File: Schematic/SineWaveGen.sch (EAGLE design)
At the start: 16 parts, among them IC1 MEGA32-P, Q1 G20N60, Q2 G20N60, Q3 H9NA80FI, Q4 H9NA80FI

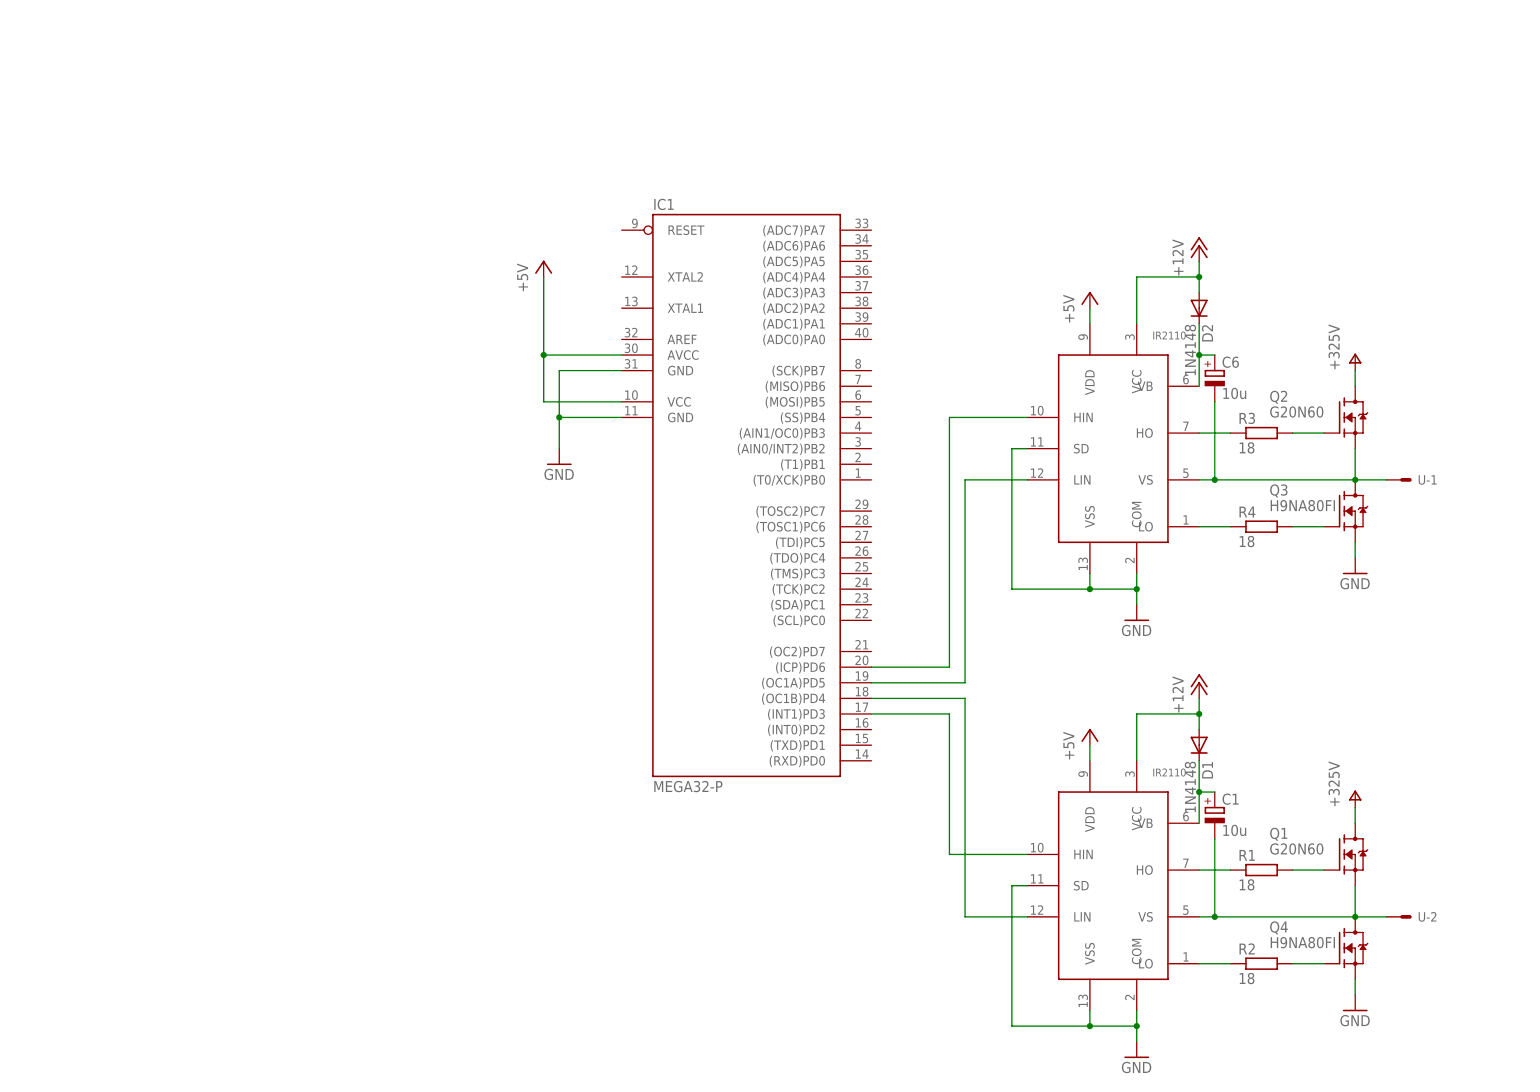
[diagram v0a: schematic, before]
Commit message: use bigger distances for high voltages
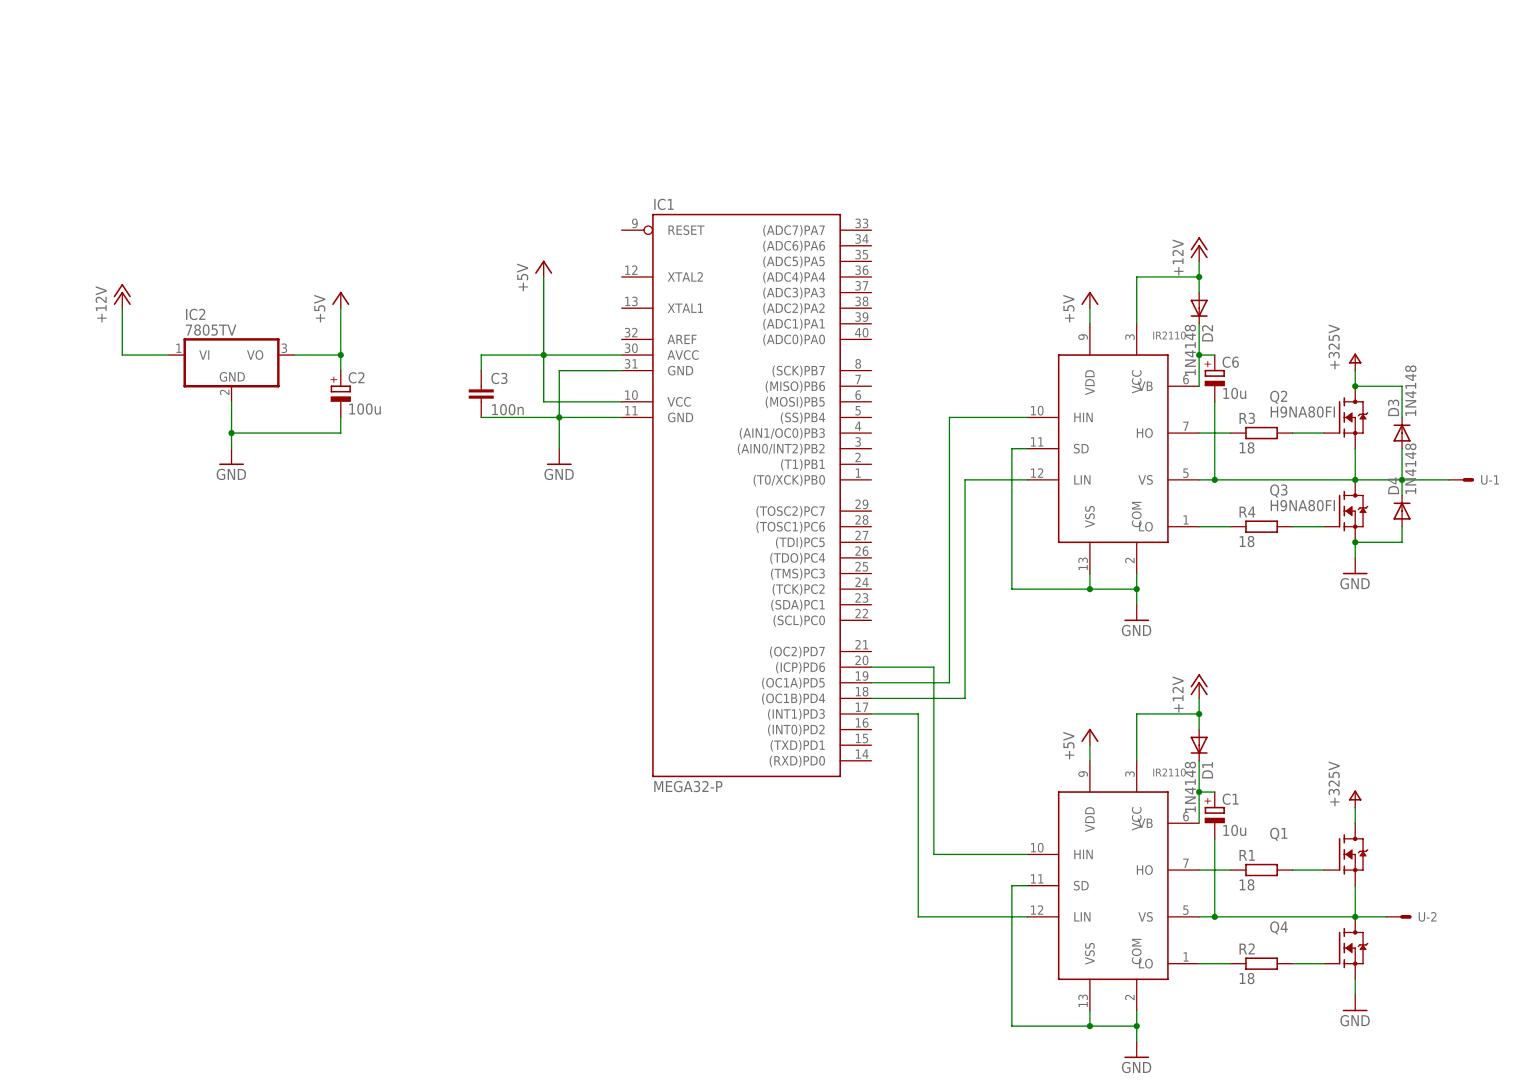
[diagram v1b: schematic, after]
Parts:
- added C2: 100u, rcl:CPOL-EUE2.5-7
- added C3: 100n, rcl:C-EU050-035X075
- added D3, D4: 1N4148, diode:1N4148DO35-7
- added IC2: 7805TV, linear:7805TV
- Q1: value G20N60 -> SPW47N60S5
- Q2: value G20N60 -> H9NA80FI
- Q4: value H9NA80FI -> SPW47N60S5
- R1: device rcl:R-EU_0207/10 -> rcl:R-EU_0207/12
- R3: device rcl:R-EU_0204/2V -> rcl:R-EU_0207/12
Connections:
- net +12V: now also IC2.VI
- net +5V: now also C2.+, C3.1, IC2.VO
- net GND: now also C2.-, C3.2, D4.A, IC2.GND
- net N$10: now also IC1.(INT1)PD3; no longer IC1.(OC1B)PD4
- net N$11: now also IC1.(ICP)PD6; no longer IC1.(INT1)PD3
- net N$2: now also IC1.(OC1B)PD4; no longer IC1.(OC1A)PD5
- net N$32: now also D3.A, D4.C
- net N$4: now also IC1.(OC1A)PD5; no longer IC1.(ICP)PD6
- net V+: now also D3.C
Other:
- moved on the sheet: U-1
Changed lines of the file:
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@@
 <setting verticaltext="up"/>
 </settings>
-<grid distance="0.1" unitdist="inch" unit="inch" style="lines" multiple="1" display="yes" altdistance="0.01" altunitdist="inch" altunit="inch"/>
+<grid distance="0.1" unitdist="inch" unit="inch" style="lines" multiple="1" display="no" altdistance="0.01" altunitdist="inch" altunit="inch"/>
 <layers>
 <layer number="1" name="Top" color="4" fill="1" visible="yes" active="no"/>
@@
 <parts>
 <part name="U$2" library="BLDC" deviceset="IR2110" device="DIL14" value="IR2110"/>
-<part name="Q2" library="transistor-fet" deviceset="SPW47N60S5" device="" value="G20N60"/>
+<part name="Q2" library="transistor-fet" deviceset="SPW47N60S5" device="" value="H9NA80FI"/>
 <part name="Q3" library="transistor-fet" deviceset="SPW47N60S5" device="" value="H9NA80FI"/>
-<part name="R3" library="rcl" deviceset="R-EU_" device="0204/2V" value="18"/>
+<part name="R3" library="rcl" deviceset="R-EU_" device="0207/12" value="18"/>
 <part name="R4" library="rcl" deviceset="R-EU_" device="0207/12" value="18"/>
 <part name="C6" library="rcl" deviceset="CPOL-EU" device="E2.5-7" value="10u"/>
@@
 <part name="P+1" library="supply1" deviceset="+5V" device=""/>
 <part name="U$1" library="BLDC" deviceset="IR2110" device="DIL14" value="IR2110"/>
-<part name="Q1" library="transistor-fet" deviceset="SPW47N60S5" device="" value="G20N60"/>
-<part name="Q4" library="transistor-fet" deviceset="SPW47N60S5" device="" value="H9NA80FI"/>
-<part name="R1" library="rcl" deviceset="R-EU_" device="0207/10" value="18"/>
+<part name="Q1" library="transistor-fet" deviceset="SPW47N60S5" device="" value=""/>
+<part name="Q4" library="transistor-fet" deviceset="SPW47N60S5" device="" value=""/>
+<part name="R1" library="rcl" deviceset="R-EU_" device="0207/12" value="18"/>
 <part name="R2" library="rcl" deviceset="R-EU_" device="0207/12" value="18"/>
 <part name="C1" library="rcl" deviceset="CPOL-EU" device="E2.5-7" value="10u"/>
@@
 <part name="GND4" library="supply1" deviceset="GND" device=""/>
 <part name="GND5" library="supply1" deviceset="GND" device=""/>
+<part name="IC2" library="linear" deviceset="78*" device="TV" technology="05"/>
+<part name="C2" library="rcl" deviceset="CPOL-EU" device="E2.5-7" value="100u"/>
+<part name="P+8" library="supply1" deviceset="+5V" device=""/>
+<part name="P+9" library="supply1" deviceset="+12V" device=""/>
+<part name="GND6" library="supply1" deviceset="GND" device=""/>
+<part name="C3" library="rcl" deviceset="C-EU" device="050-035X075" value="100n"/>
+<part name="D3" library="diode" deviceset="1N4148" device="DO35-7" value="1N4148"/>
+<part name="D4" library="diode" deviceset="1N4148" device="DO35-7" value="1N4148"/>
 </parts>
 <sheets>
@@
 <instance part="R4" gate="G$1" x="58.42" y="60.96"/>
 <instance part="C6" gate="G$1" x="50.8" y="86.36"/>
-<instance part="U" gate="-1" x="81.28" y="68.58"/>
+<instance part="U" gate="-1" x="91.44" y="68.58"/>
 <instance part="U" gate="-2" x="81.28" y="-2.54"/>
 <instance part="IC1" gate="G$1" x="-25.4" y="66.04"/>
@@
 <instance part="GND4" gate="1" x="73.66" y="-17.78"/>
 <instance part="GND5" gate="1" x="38.1" y="-25.4"/>
+<instance part="IC2" gate="A1" x="-109.22" y="88.9"/>
+<instance part="C2" gate="G$1" x="-91.44" y="83.82"/>
+<instance part="P+8" gate="1" x="-91.44" y="99.06"/>
+<instance part="P+9" gate="1" x="-127" y="99.06"/>
+<instance part="GND6" gate="1" x="-109.22" y="71.12"/>
+<instance part="C3" gate="G$1" x="-68.58" y="83.82"/>
+<instance part="D3" gate="G$1" x="81.28" y="76.2" rot="R90"/>
+<instance part="D4" gate="G$1" x="81.28" y="63.5" rot="R90"/>
 </instances>
 <busses>
@@
 <pinref part="U$2" gate="G$1" pin="VS"/>
 <pinref part="U" gate="-1" pin="S"/>
-<wire x1="78.74" y1="68.58" x2="73.66" y2="68.58" width="0.1524" layer="91"/>
+<wire x1="88.9" y1="68.58" x2="81.28" y2="68.58" width="0.1524" layer="91"/>
+<pinref part="D4" gate="G$1" pin="C"/>
+<wire x1="81.28" y1="68.58" x2="73.66" y2="68.58" width="0.1524" layer="91"/>
+<wire x1="81.28" y1="66.04" x2="81.28" y2="68.58" width="0.1524" layer="91"/>
+<junction x="81.28" y="68.58"/>
+<pinref part="D3" gate="G$1" pin="A"/>
+<wire x1="81.28" y1="73.66" x2="81.28" y2="68.58" width="0.1524" layer="91"/>
 </segment>
 </net>
@@
 <pinref part="U$2" gate="G$1" pin="LIN"/>
 <wire x1="20.32" y1="68.58" x2="10.16" y2="68.58" width="0.1524" layer="91"/>
-<wire x1="10.16" y1="68.58" x2="10.16" y2="35.56" width="0.1524" layer="91"/>
-<pinref part="IC1" gate="G$1" pin="(OC1A)PD5"/>
-<wire x1="-5.08" y1="35.56" x2="10.16" y2="35.56" width="0.1524" layer="91"/>
+<wire x1="10.16" y1="68.58" x2="10.16" y2="33.02" width="0.1524" layer="91"/>
+<pinref part="IC1" gate="G$1" pin="(OC1B)PD4"/>
+<wire x1="-5.08" y1="33.02" x2="10.16" y2="33.02" width="0.1524" layer="91"/>
 </segment>
 </net>
@@
 <pinref part="U$2" gate="G$1" pin="HIN"/>
 <wire x1="20.32" y1="78.74" x2="7.62" y2="78.74" width="0.1524" layer="91"/>
-<wire x1="7.62" y1="78.74" x2="7.62" y2="38.1" width="0.1524" layer="91"/>
-<pinref part="IC1" gate="G$1" pin="(ICP)PD6"/>
-<wire x1="7.62" y1="38.1" x2="-5.08" y2="38.1" width="0.1524" layer="91"/>
+<wire x1="7.62" y1="78.74" x2="7.62" y2="35.56" width="0.1524" layer="91"/>
+<pinref part="IC1" gate="G$1" pin="(OC1A)PD5"/>
+<wire x1="-5.08" y1="35.56" x2="7.62" y2="35.56" width="0.1524" layer="91"/>
 </segment>
 </net>
@@
 <pinref part="Q3" gate="G$1" pin="S"/>
 <pinref part="GND2" gate="1" pin="GND"/>
+<pinref part="D4" gate="G$1" pin="A"/>
+<wire x1="73.66" y1="58.42" x2="81.28" y2="58.42" width="0.1524" layer="91"/>
+<wire x1="81.28" y1="58.42" x2="81.28" y2="60.96" width="0.1524" layer="91"/>
+<junction x="73.66" y="58.42"/>
 </segment>
 <segment>
@@
 <junction x="-55.88" y="78.74"/>
 <pinref part="GND1" gate="1" pin="GND"/>
+<pinref part="C3" gate="G$1" pin="2"/>
+<wire x1="-55.88" y1="78.74" x2="-68.58" y2="78.74" width="0.1524" layer="91"/>
 </segment>
 <segment>
@@
 <junction x="30.48" y="-20.32"/>
 </segment>
+<segment>
+<pinref part="C2" gate="G$1" pin="-"/>
+<wire x1="-91.44" y1="78.74" x2="-91.44" y2="76.2" width="0.1524" layer="91"/>
+<pinref part="IC2" gate="A1" pin="GND"/>
+<wire x1="-91.44" y1="76.2" x2="-109.22" y2="76.2" width="0.1524" layer="91"/>
+<wire x1="-109.22" y1="76.2" x2="-109.22" y2="81.28" width="0.1524" layer="91"/>
+<pinref part="GND6" gate="1" pin="GND"/>
+<wire x1="-109.22" y1="76.2" x2="-109.22" y2="73.66" width="0.1524" layer="91"/>
+<junction x="-109.22" y="76.2"/>
+</segment>
 </net>
 <net name="+5V" class="0">
@@
 <junction x="-58.42" y="88.9"/>
 <pinref part="P+1" gate="1" pin="+5V"/>
+<pinref part="C3" gate="G$1" pin="1"/>
+<wire x1="-58.42" y1="88.9" x2="-68.58" y2="88.9" width="0.1524" layer="91"/>
+<wire x1="-68.58" y1="88.9" x2="-68.58" y2="86.36" width="0.1524" layer="91"/>
 </segment>
 <segment>
@@
 <wire x1="30.48" y1="25.4" x2="30.48" y2="22.86" width="0.1524" layer="91"/>
 <pinref part="P+6" gate="1" pin="+5V"/>
+</segment>
+<segment>
+<pinref part="P+8" gate="1" pin="+5V"/>
+<pinref part="C2" gate="G$1" pin="+"/>
+<wire x1="-91.44" y1="96.52" x2="-91.44" y2="88.9" width="0.1524" layer="91"/>
+<pinref part="IC2" gate="A1" pin="VO"/>
+<wire x1="-91.44" y1="88.9" x2="-91.44" y2="86.36" width="0.1524" layer="91"/>
+<wire x1="-99.06" y1="88.9" x2="-91.44" y2="88.9" width="0.1524" layer="91"/>
+<junction x="-91.44" y="88.9"/>
 </segment>
 </net>
@@
 <junction x="48.26" y="30.48"/>
 </segment>
+<segment>
+<pinref part="IC2" gate="A1" pin="VI"/>
+<pinref part="P+9" gate="1" pin="+12V"/>
+<wire x1="-119.38" y1="88.9" x2="-127" y2="88.9" width="0.1524" layer="91"/>
+<wire x1="-127" y1="88.9" x2="-127" y2="96.52" width="0.1524" layer="91"/>
+</segment>
 </net>
 <net name="V+" class="0">
@@
 <pinref part="P+5" gate="1" pin="V+"/>
 <wire x1="73.66" y1="83.82" x2="73.66" y2="86.36" width="0.1524" layer="91"/>
+<pinref part="D3" gate="G$1" pin="C"/>
+<wire x1="81.28" y1="78.74" x2="81.28" y2="83.82" width="0.1524" layer="91"/>
+<wire x1="81.28" y1="83.82" x2="73.66" y2="83.82" width="0.1524" layer="91"/>
+<junction x="73.66" y="83.82"/>
 </segment>
 <segment>
@@
 <segment>
 <pinref part="U$1" gate="G$1" pin="LIN"/>
-<wire x1="20.32" y1="-2.54" x2="10.16" y2="-2.54" width="0.1524" layer="91"/>
-<pinref part="IC1" gate="G$1" pin="(OC1B)PD4"/>
-<wire x1="-5.08" y1="33.02" x2="10.16" y2="33.02" width="0.1524" layer="91"/>
-<wire x1="10.16" y1="33.02" x2="10.16" y2="-2.54" width="0.1524" layer="91"/>
+<wire x1="20.32" y1="-2.54" x2="2.54" y2="-2.54" width="0.1524" layer="91"/>
+<pinref part="IC1" gate="G$1" pin="(INT1)PD3"/>
+<wire x1="-5.08" y1="30.48" x2="2.54" y2="30.48" width="0.1524" layer="91"/>
+<wire x1="2.54" y1="30.48" x2="2.54" y2="-2.54" width="0.1524" layer="91"/>
 </segment>
 </net>
@@
 <segment>
 <pinref part="U$1" gate="G$1" pin="HIN"/>
-<wire x1="20.32" y1="7.62" x2="7.62" y2="7.62" width="0.1524" layer="91"/>
-<wire x1="7.62" y1="7.62" x2="7.62" y2="30.48" width="0.1524" layer="91"/>
-<pinref part="IC1" gate="G$1" pin="(INT1)PD3"/>
-<wire x1="7.62" y1="30.48" x2="-5.08" y2="30.48" width="0.1524" layer="91"/>
-</segment>
-</net>
+<wire x1="20.32" y1="7.62" x2="5.08" y2="7.62" width="0.1524" layer="91"/>
+<pinref part="IC1" gate="G$1" pin="(ICP)PD6"/>
+<wire x1="-5.08" y1="38.1" x2="5.08" y2="38.1" width="0.1524" layer="91"/>
+<wire x1="5.08" y1="38.1" x2="5.08" y2="7.62" width="0.1524" layer="91"/>
+</segment>
+</net>

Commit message: Make it possible to choose a trapez generator
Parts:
- removed IC1: MEGA32-P, atmel:MEGA32-P
- added C4: 100n, rcl:C-EU050-035X075
- added C5, C7: 100u, rcl:CPOL-EUE2.5-7
- added D5, D6: 1N4148, diode:1N4148DO35-7
- added IC3: MEGA8515-P, atmel:MEGA8515-P
- added SV1: (no value), con-lstb:MA03-1
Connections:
- new net N$12: IC3.PE2(OC1B), U$2.LIN
- new net N$3: IC3.(OC1A)PD5, U$1.LIN
- net +12V: now also C5.+, C7.+
- net +5V: now also C4.1, IC3.VCC; no longer IC1.AVCC, IC1.VCC
- net GND: now also C4.2, C5.-, C7.-, D5.A, IC3.GND, SV1.1; no longer IC1.GND, IC1.GND@1
- net N$10: now also IC3.(TXD)PD1, SV1.2; no longer IC1.(INT1)PD3, U$1.LIN
- net N$11: now also IC3.(RXD)PD0, SV1.3; no longer IC1.(ICP)PD6, U$1.HIN
- net N$2: now also IC3.(AD0)PA0, U$2.HIN; no longer IC1.(OC1B)PD4, U$2.LIN
- net N$4: now also IC3.(A12)PC4, U$1.HIN; no longer IC1.(OC1A)PD5, U$2.HIN
- net N$6: now also D5.C, D6.A
- net V+: now also D6.C
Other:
- moved on the sheet: C2, C3, IC2, U-2
